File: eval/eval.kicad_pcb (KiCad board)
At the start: 4 copper layers, 49.2 x 98 mm, 163 parts, among them CN1 XT30PW-M, J1 TC2030, Q1 BSC0702LS, Q10 2N7002, Q2 BSC0702LS, Q3 AP40P04Q, Q4 DMG2302UK-7, Q5 BSC0702LS, Q6 BSC0702LS, Q7 WSD4070DN, Q8 WSD4070DN, Q9 2N7002, U1 AP63205WU-7, U10 TPS7A2033PDBVR, U11 RCLAMP0521T-ES, U12 TPS7A2033PDBVR, U13 RCLAMP0521T-ES, U14 TLV9061xDBV, U15 TCAN1044VDRBRQ1, U16 MX74700T_C22468156, U17 MX74700T_C22468156, U18 TLV3501AIDBV, U19 TLV9062, U2 LM5148RGYR, U20 LM2903, U22 SN74LVC1G00DBV, U23 SN74LVC1G00DBV, U24 HYG015N03LS1C2, U25 HYG015N03LS1C2, U3 INA180A3, U4 HUSB238A-BB001-QN16R, U6 HS096T01H13, U7 MX74502D23_C41433189, U8 INA180A3, U9 STM32G0B1CBTx

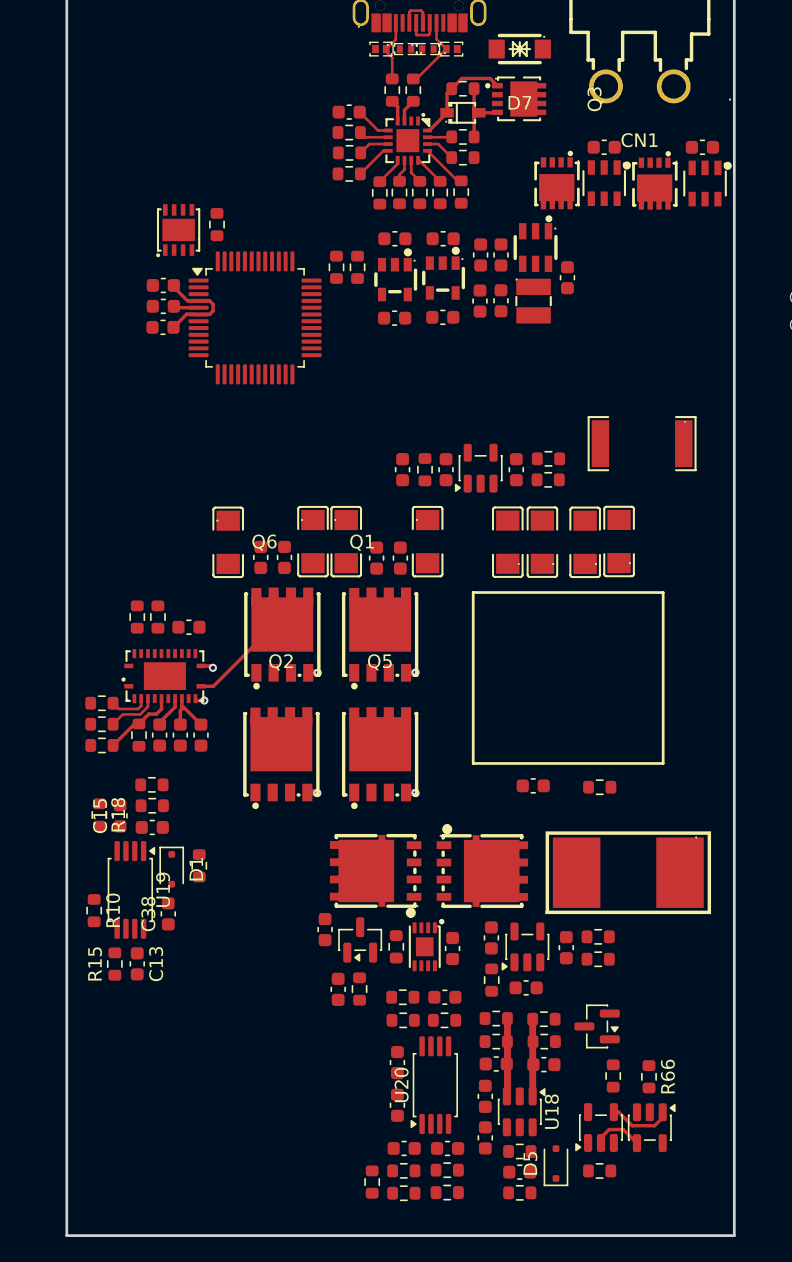
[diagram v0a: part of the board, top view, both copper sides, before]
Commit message: [layout] group every function group together, ready for layout
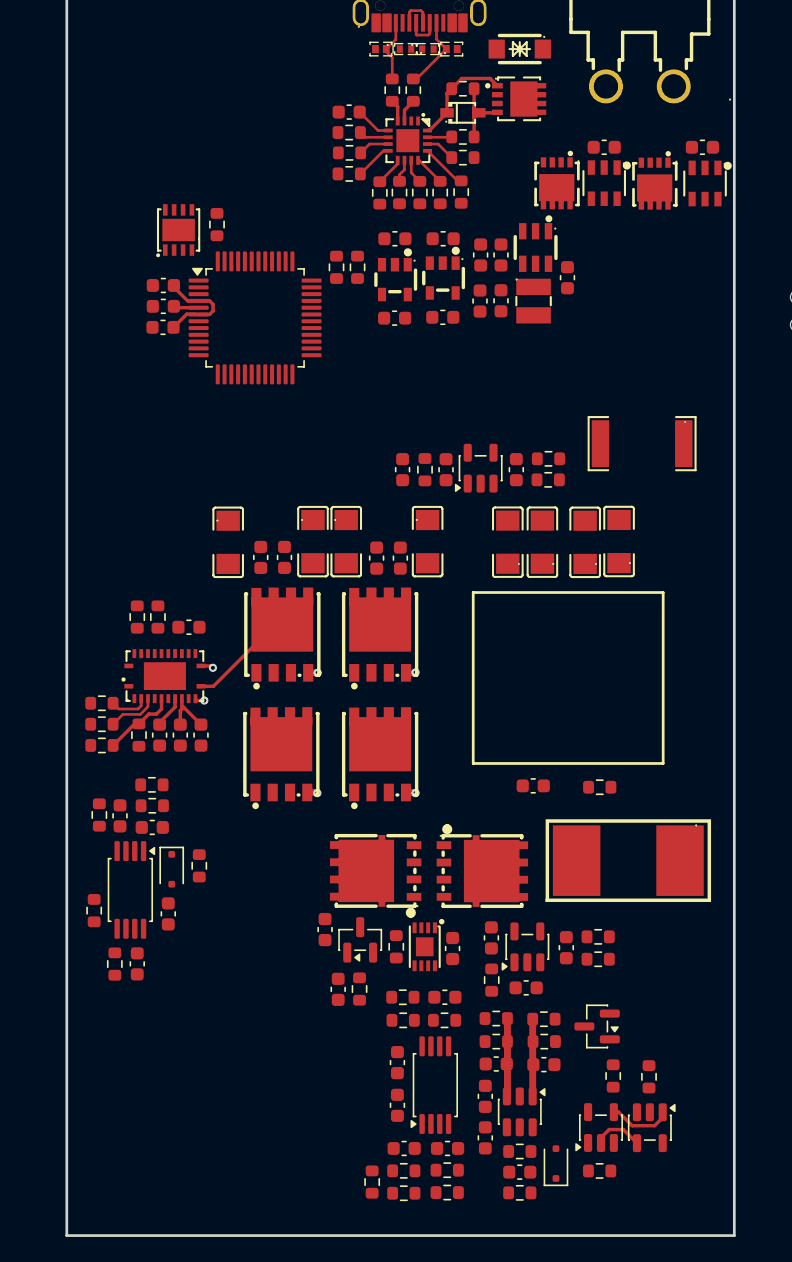
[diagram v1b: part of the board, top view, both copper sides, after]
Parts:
- moved R46 0.89 mm to (75.4, 128.0)
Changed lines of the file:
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@@
 			(at 0 -1.85 90)
 			(layer "F.SilkS")
+			(hide yes)
 			(effects
 				(font
@@
 			(at 0 -2.45 90)
 			(layer "F.SilkS")
+			(hide yes)
 			(effects
 				(font
@@
 			(at 0 -1.85 90)
 			(layer "F.SilkS")
+			(hide yes)
 			(effects
 				(font
@@
 			(at -1.31 -6.819 0)
 			(layer "F.SilkS")
+			(hide yes)
 			(effects
 				(font
@@
 			(at 0 -1.43 90)
 			(layer "F.SilkS")
+			(hide yes)
 			(effects
 				(font
@@
 			(at 0 -1.43 90)
 			(layer "F.SilkS")
+			(hide yes)
 			(effects
 				(font
@@
 	(footprint "EasyEDA:R3920"
 		(layer "F.Cu")
-		(at 75.438 128.905 180)
+		(at 75.438 128.016 180)
 		(property "Reference" "R46"
 			(at 0 -4 0)
@@
 			(at 0 -2.45 90)
 			(layer "F.SilkS")
+			(hide yes)
 			(effects
 				(font
@@
 			(at 0 -6.819 0)
 			(layer "F.SilkS")
+			(hide yes)
 			(effects
 				(font
@@
 			(at 0 -1.43 90)
 			(layer "F.SilkS")
+			(hide yes)
 			(effects
 				(font
@@
 			(at 0 -1.43 90)
 			(layer "F.SilkS")
+			(hide yes)
 			(effects
 				(font
@@
 			(at 0 -1.43 90)
 			(layer "F.SilkS")
+			(hide yes)
 			(effects
 				(font
@@
 			(at 0 -5.6 90)
 			(layer "F.SilkS")
+			(hide yes)
 			(effects
 				(font
@@
 			(at 0 -4 0)
 			(layer "F.SilkS")
+			(hide yes)
 			(effects
 				(font
@@
 			(at 0 -1.43 90)
 			(layer "F.SilkS")
+			(hide yes)
 			(effects
 				(font
@@
 			(at 0 -6.819 0)
 			(layer "F.SilkS")
+			(hide yes)
 			(effects
 				(font
@@
 			(at 0 -9 0)
 			(layer "F.SilkS")
+			(hide yes)
 			(effects
 				(font
@@
 			(at -1.31 -6.819 0)
 			(layer "F.SilkS")
+			(hide yes)
 			(effects
 				(font
@@
 			(at 0 -1.43 90)
 			(layer "F.SilkS")
+			(hide yes)
 			(effects
 				(font
@@
 			(at 0 -2.4 90)
 			(layer "F.SilkS")
+			(hide yes)
 			(effects
 				(font
@@
 	)
 	(gr_rect
-		(start 37.422 69.254)
-		(end 58.422 139.254)
+		(start 36.109 81.407)
+		(end 57.109 151.407)
 		(stroke
 			(width 0.1)

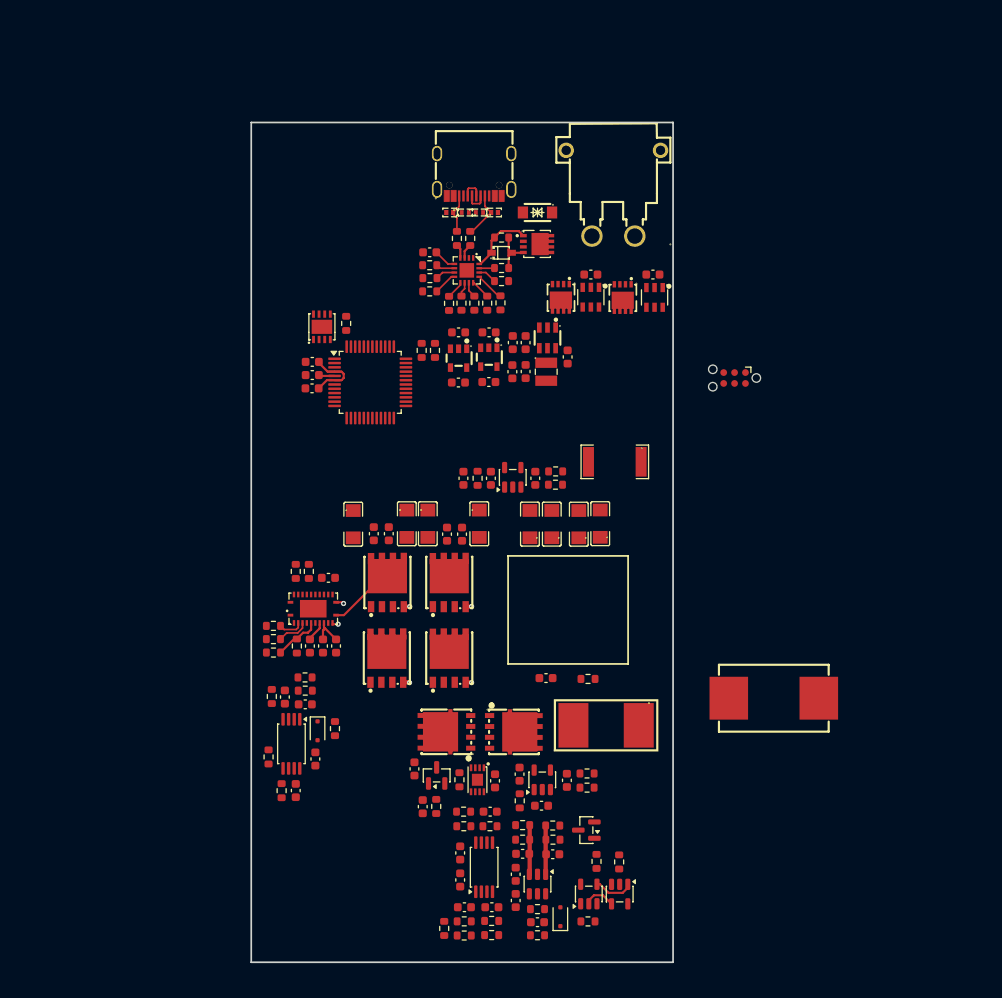
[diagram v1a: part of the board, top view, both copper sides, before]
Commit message: [layout] fan on bottom side, power area on top
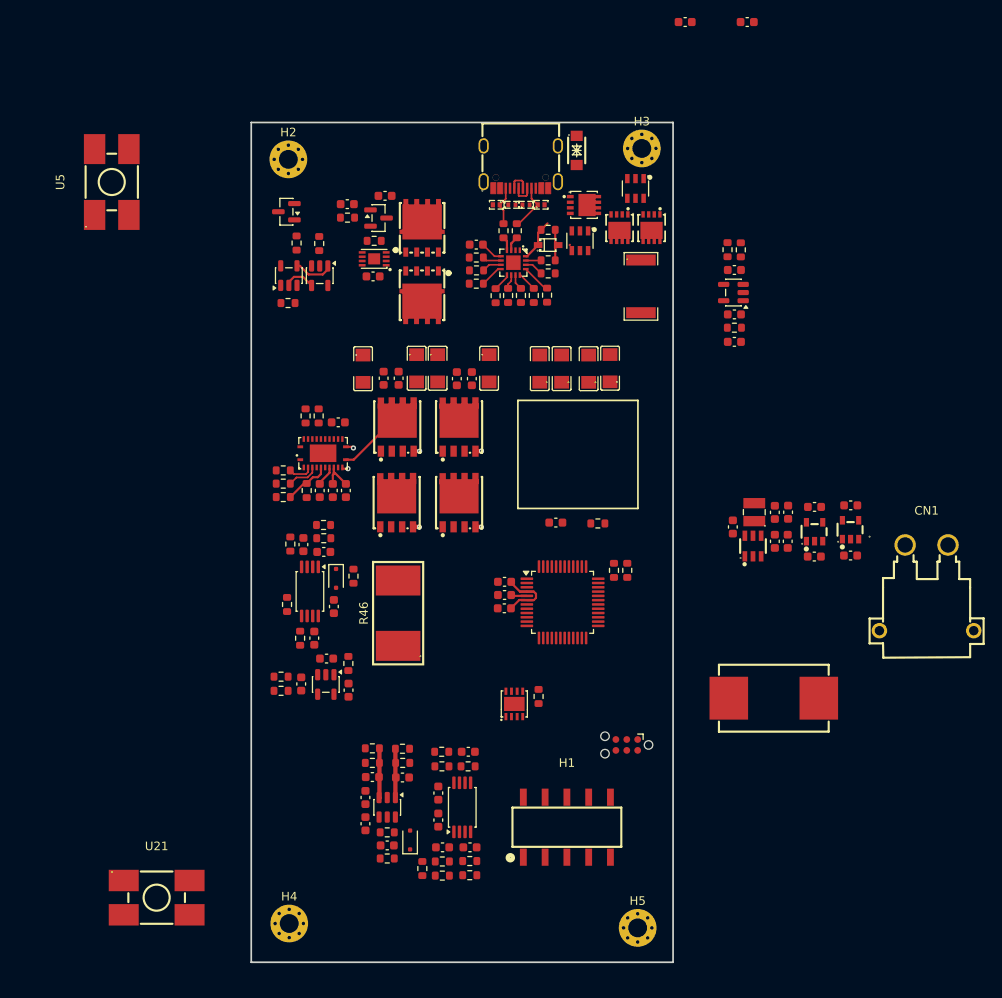
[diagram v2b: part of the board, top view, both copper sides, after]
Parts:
- added H1: 2.54-2*5P, EasyEDA:HDR-SMD_10P-P2.54-V-F-R2-C5-S2.54-LS7.4, F.Cu at (70.9, 139.9)
- added H2: MountingHole_Pad, MountingHole:MountingHole_2.2mm_M2_Pad_Via, F.Cu at (38.4, 62.0)
- added H3: MountingHole_Pad, MountingHole:MountingHole_2.2mm_M2_Pad_Via, F.Cu at (79.6, 60.7)
- added H4: MountingHole_Pad, MountingHole:MountingHole_2.2mm_M2_Pad_Via, F.Cu at (38.5, 151.1)
- added H5: MountingHole_Pad, MountingHole:MountingHole_2.2mm_M2_Pad_Via, F.Cu at (79.1, 151.6)
- added U21: TS34031, EasyEDA:CONN-SMD_TS34031, F.Cu at (23.0, 148.1)
- added U5: TS34031, EasyEDA:CONN-SMD_TS34031, F.Cu at (17.8, 64.6)
- moved R66 80.2 mm to (42.0, 71.8)
- moved U22 80.2 mm to (38.4, 75.6)
- moved Q9 80.2 mm to (38.1, 68.1)
- moved R56 80.2 mm to (39.3, 71.8)
- moved R65 80.2 mm to (38.3, 78.8)
- moved U23 80.2 mm to (42.0, 75.6)
- moved C61 70.8 mm to (45.3, 67.2), turned to 0 degrees
- moved R64 69.5 mm to (45.3, 68.8), turned to 180 degrees
- moved C50 66.9 mm to (49.7, 66.3), turned to 180 degrees
- moved Q10 65.4 mm to (48.9, 68.8), turned to 0 degrees
- moved R58 63.6 mm to (48.4, 71.5), turned to 180 degrees
- moved U7 61.9 mm to (48.4, 73.6), turned to 90 degrees
- moved C49 60.5 mm to (48.3, 75.7), turned to 180 degrees
- moved U25 58.9 mm to (54.0, 70.0), turned to 0 degrees
- moved CN1 58.8 mm to (112.8, 112.0), turned to 0 degrees
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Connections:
- C40 pad 1: /power_buck/OUT_ISNS+ -> /power_buck/VOUT
- C41 pad 1: /power_buck/OUT_ISNS+ -> /power_buck/VOUT
- C42 pad 1: /power_buck/OUT_ISNS+ -> /power_buck/VOUT
- C43 pad 1: /power_buck/OUT_ISNS+ -> /power_buck/VOUT
- C49 pad 1: /power_buck/OUT_ISNS- -> /power_buck/VOUT
- L1 pad 1: /power_buck/OUT_ISNS+ -> /power_buck/VOUT
- R14 pad 1: /power_buck/OUT_ISNS- -> GNDPWR
- R45 pad 2: /power_buck/OUT_ISNS+ -> /power_buck/VOUT
- R46 pad 1: /power_buck/OUT_ISNS+ -> GNDPWR
- R46 pad 2: /power_buck/OUT_ISNS- -> /power_buck/OUT_ISNS+
- R6 pad 1: /power_buck/OUT_ISNS- -> /power_buck/VOUT
- U2 pad 21: /power_buck/OUT_ISNS+ -> /power_buck/VOUT
- U24 pad 5: /power_buck/OUT_ISNS- -> /power_buck/VOUT
- U24 pad 6: /power_buck/OUT_ISNS- -> /power_buck/VOUT
- U24 pad 7: /power_buck/OUT_ISNS- -> /power_buck/VOUT
- U24 pad 8: /power_buck/OUT_ISNS- -> /power_buck/VOUT
- U24 pad 9: /power_buck/OUT_ISNS- -> /power_buck/VOUT
- U7 pad 1: /power_buck/OUT_ISNS- -> /power_buck/VOUT
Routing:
- net Net-(D4-K): track 7.79 -> 4.96 mm
- net Net-(D4-A): track 5.23 -> 3.84 mm

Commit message: Update eval.kicad_pcb
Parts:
- moved Q9 85.7 mm to (69.3, 147.9), turned to 90 degrees
- moved R66 83.4 mm to (65.6, 151.8), turned to 180 degrees
- moved R56 81.7 mm to (65.7, 149.1), turned to 0 degrees
- moved U23 78.8 mm to (61.8, 151.8), turned to 180 degrees
- moved U22 76.3 mm to (61.9, 148.2), turned to 0 degrees
- moved C61 74.9 mm to (56.2, 141.3), turned to 90 degrees
- moved R64 73.6 mm to (57.8, 141.3), turned to -90 degrees
- moved R65 72.3 mm to (58.7, 148.1), turned to 90 degrees
- moved C50 70.9 mm to (55.2, 136.9), turned to -90 degrees
- moved Q10 69.4 mm to (57.8, 137.7), turned to 90 degrees
- moved R58 67.8 mm to (60.5, 138.2), turned to -90 degrees
- moved U7 66.1 mm to (62.6, 138.2), turned to 180 degrees
- moved C49 64.8 mm to (64.6, 138.3), turned to -90 degrees
- moved U25 62.8 mm to (59.0, 132.6), turned to 90 degrees
- moved CN1 59.8 mm to (74.4, 66.2), turned to 180 degrees
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
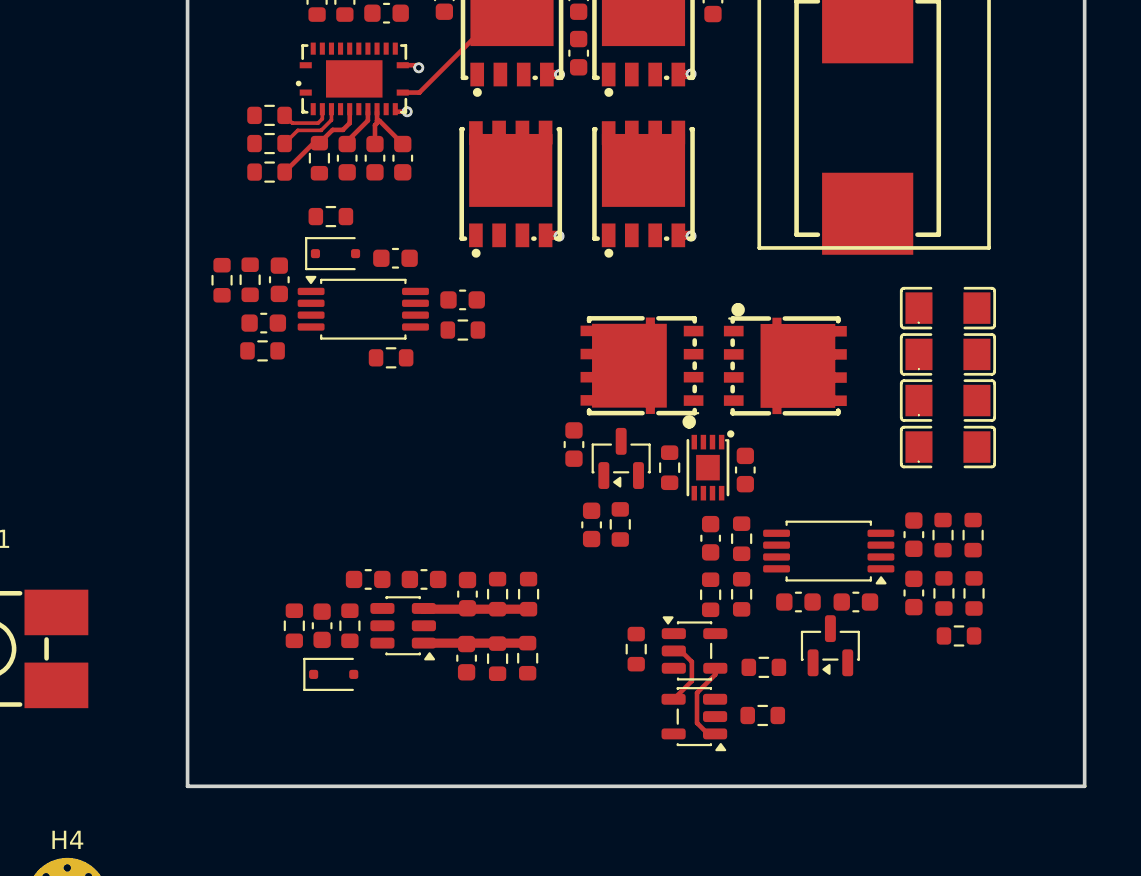
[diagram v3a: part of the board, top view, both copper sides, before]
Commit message: [layout] buck in bottom first commit
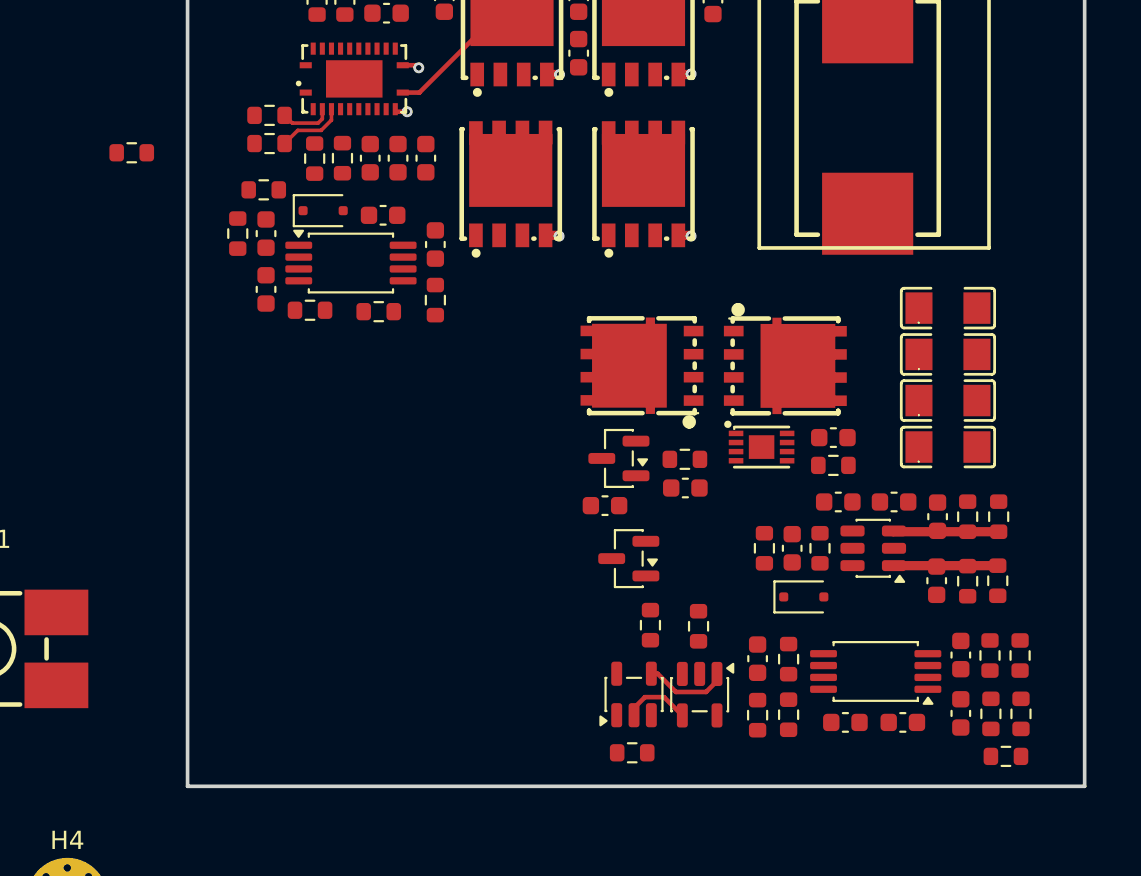
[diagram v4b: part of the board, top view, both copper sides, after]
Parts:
- moved C51 26.1 mm to (75.1, 144.4)
- moved C52 26.1 mm to (75.2, 140.9)
- moved C54 26.1 mm to (72.8, 140.1)
- moved D5 26.1 mm to (67.8, 145.3)
- moved U18 26.1 mm to (71.7, 142.6)
- moved C53 26.1 mm to (67.2, 142.6)
- moved C55 26.1 mm to (69.7, 140.1)
- moved R16 26.1 mm to (78.5, 144.4)
- moved R19 26.1 mm to (76.8, 144.4)
- moved R25 26.1 mm to (78.5, 140.9)
- moved R48 26.1 mm to (76.8, 140.9)
- moved R49 26.1 mm to (68.7, 142.6)
- moved R50 26.1 mm to (65.7, 142.6)
- moved Q9 12.0 mm to (58.2, 143.2), turned to 180 degrees
- moved R58 8.98 mm to (69.5, 138.0), turned to 180 degrees
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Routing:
- net /power_buck/FB: track 5.31 -> 0.15 mm
- net Net-(U2-VCC): track 3.76 -> 0.00 mm
- net Net-(U2-VDDA): track 2.25 -> 0.00 mm

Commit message: [layout] layout completed, ready for trace
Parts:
- added JP1: SolderJumper_2_Bridged, Jumper:SolderJumper-2_P1.3mm_Bridged_RoundedPad1.0x1.5mm, B.Cu at (90.2, 141.7)
- added JP2: SolderJumper_2_Bridged, Jumper:SolderJumper-2_P1.3mm_Bridged_RoundedPad1.0x1.5mm, B.Cu at (90.2, 145.3)
- added JP3: SolderJumper_2_Bridged, Jumper:SolderJumper-2_P1.3mm_Bridged_RoundedPad1.0x1.5mm, B.Cu at (90.2, 148.8)
- added JP4: SolderJumper_2_Bridged, Jumper:SolderJumper-2_P1.3mm_Bridged_RoundedPad1.0x1.5mm, B.Cu at (90.2, 152.4)
- added TP1: neg_volt, TestPoint:TestPoint_Pad_D2.0mm, B.Cu at (29.3, 131.1)
- added TP2: over_current, TestPoint:TestPoint_Pad_D2.0mm, B.Cu at (29.3, 135.1)
- added TP4: drop_volt, TestPoint:TestPoint_Pad_D2.0mm, B.Cu at (25.3, 131.1)
- added TP5: fault_latch, TestPoint:TestPoint_Pad_D2.0mm, B.Cu at (25.3, 135.1)
- added TP6: power_on_hold_rc, TestPoint:TestPoint_Pad_D2.0mm, B.Cu at (21.2, 131.1)
- added TP7: 74502_en, TestPoint:TestPoint_Pad_D2.0mm, B.Cu at (21.2, 135.1)
- added TP8: 74502_ov, TestPoint:TestPoint_Pad_D2.0mm, B.Cu at (17.2, 131.1)
- added TP9: fault_reset_mcu, TestPoint:TestPoint_Pad_D2.0mm, B.Cu at (17.2, 135.1)
- moved C28 50.6 mm to (54.6, 91.3), turned to 90 degrees
- moved U10 48.5 mm to (57.4, 91.3), turned to 0 degrees
- moved C29 47.5 mm to (54.7, 87.5), turned to 90 degrees
- moved C26 46.7 mm to (60.5, 91.3), turned to -90 degrees
- moved U12 45.9 mm to (57.6, 87.5), turned to 0 degrees
- moved J1 45.6 mm to (76.3, 83.2), turned to 90 degrees
- moved C27 44.5 mm to (60.5, 87.5), turned to -90 degrees
- moved C24 38.4 mm to (66.3, 79.7), turned to 0 degrees
- moved C16 38.0 mm to (69.7, 79.7), turned to 0 degrees
- moved C23 36.2 mm to (66.3, 81.2), turned to 0 degrees
- moved C22 35.9 mm to (69.7, 81.2), turned to 0 degrees
- moved L3 32.9 mm to (66.3, 83.6), turned to 180 degrees
- moved U1 32.3 mm to (70.2, 83.8), turned to 90 degrees
- moved C14 29.1 mm to (68.0, 86.1), turned to 180 degrees
- moved R25 26.1 mm to (53.0, 146.3), turned to 90 degrees
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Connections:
- C53 pad 1: /power_battery/OV -> Net-(D5-K)
- D5 pad 1: /power_battery/OV -> Net-(D5-K)
- Q9 pad 3: /power_battery/power_on_hold -> Net-(JP4-A)
- R50 pad 1: /power_battery/OV -> Net-(D5-K)
- U20 pad 1: /power_battery/power_on_hold -> Net-(JP2-A)
- U20 pad 7: /power_battery/power_on_hold -> Net-(JP3-A)
